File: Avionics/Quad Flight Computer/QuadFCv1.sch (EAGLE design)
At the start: 94 parts, among them J1 10104111_MICROUSBAB, J2 1050270001, SW1 2-1437565-9, U1 TM4C123GH6PZ, U2 74LVC4245APW, U3 ATMEGA32U2-MU, U4 SPI_PPM, U5 MPU-6000, U6 HMC5883LSMD, U7 MS5611-01BA, U8 74AUP1G19GW, U9 S25FL127S, X1 HWB, Y1 32.768KHZ, Y2 AWSCR-20.00CW-T, Y3 PRQC16.00SR5010X000

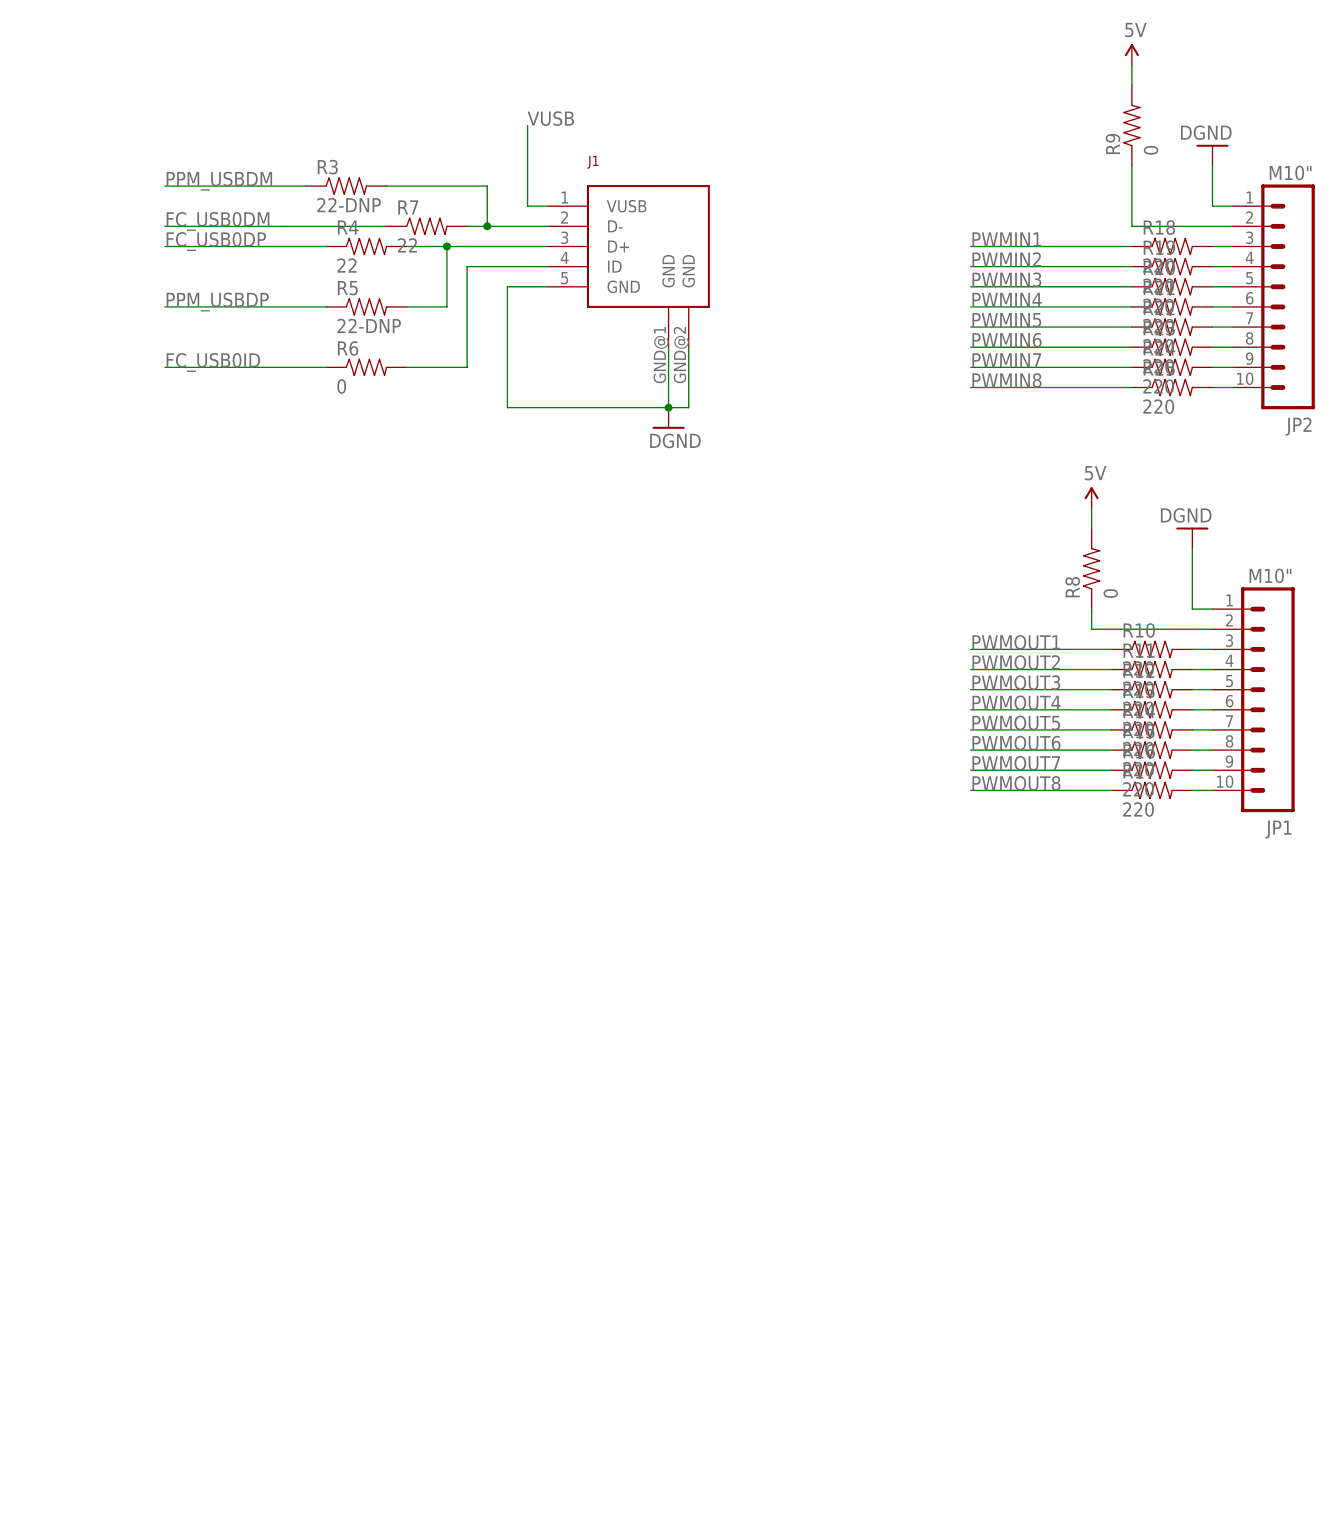
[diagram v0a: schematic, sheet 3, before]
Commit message: Added several connectors and modified power inputs to not immediately go to 5V plane.
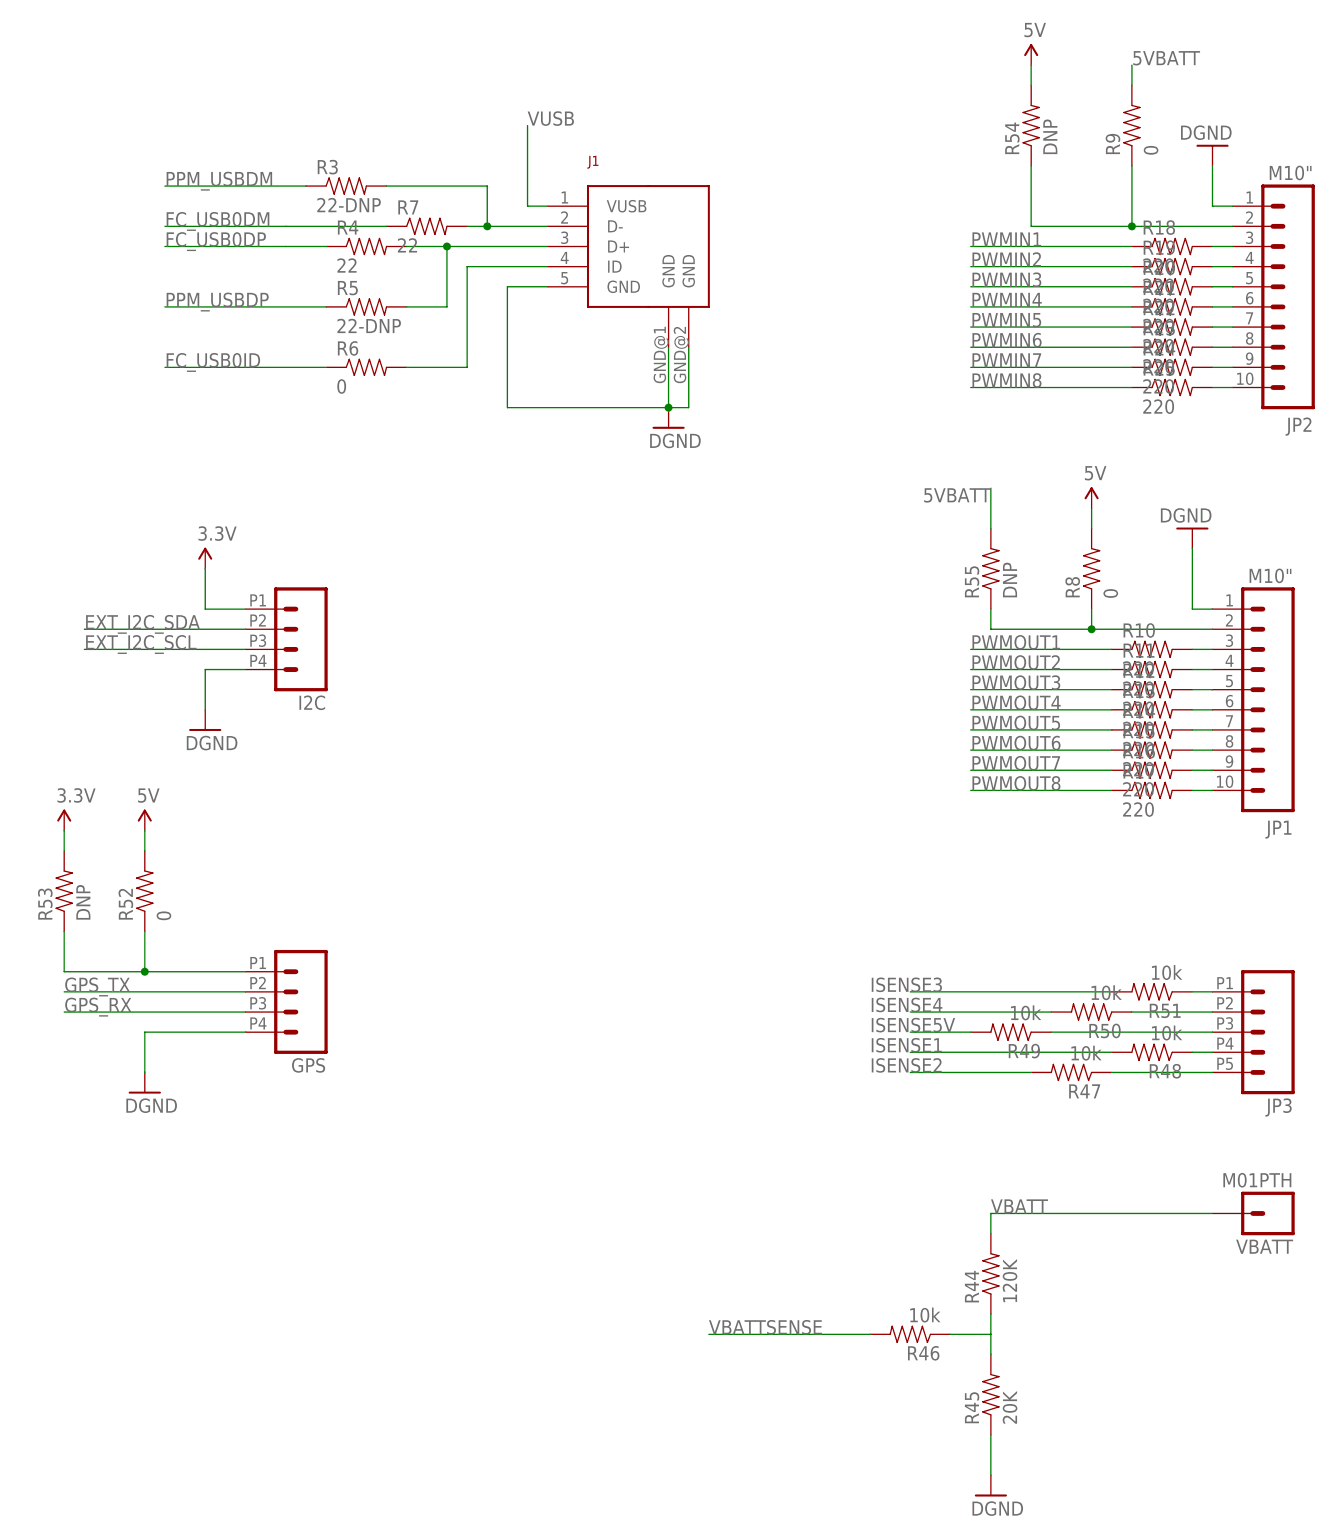
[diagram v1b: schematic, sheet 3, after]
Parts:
- added FC_JTAG: M04X2, SparkFun-Connectors:M04X2
- added GPS, I2C: (no value), Shared Libraries:M04DF13
- added JP3: (no value), Shared Libraries:M05DF13
- added R44: 120K, Shared Libraries:RESISTOR0603-RES
- added R45: 20K, Shared Libraries:RESISTOR0603-RES
- added R46, R47, R48, R49, R50, R51: 10k, Shared Libraries:RESISTOR0603-RES
- added R52: 0, Shared Libraries:RESISTOR0603-RES
- added R53: DNP, Shared Libraries:RESISTOR0603-RES
- added R54, R55: DNP, SparkFun-Resistors:RESISTOR0805-RES
- added VBATT: M01PTH, SparkFun-Connectors:M01PTH
- C15, C16, C17, C18: device SparkFun:CAP0402-CAP -> SparkFun:CAP0402
- R28, R29, R30, R31, R32, R33, R34, R35, R36, R37: device SparkFun:RESISTOR0402-RES -> SparkFun:RESISTOR0402
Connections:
- new net 5VBATT: R55.2, R9.2
- new net EXT_I2C_SCL: I2C.3
- new net EXT_I2C_SDA: I2C.2
- new net GPS_RX: GPS.3
- new net GPS_TX: GPS.2
- new net ISENSE1: R48.2
- new net ISENSE2: R47.2
- new net ISENSE3: R51.2
- new net ISENSE4: R50.2
- new net ISENSE5V: R49.2
- new net N$38: R44.1, R45.2, R46.1
- new net N$39: GPS.1, R52.1, R53.1
- new net N$44: JP3.1, R51.1
- new net N$45: JP3.2, R50.1
- new net N$46: JP3.3, R49.1
- new net N$47: JP3.4, R48.1
- new net N$48: JP3.5, R47.1
- new net VBATT: R44.2, VBATT.1
- new net VBATTSENSE: R46.2
- net 3.3V: now also FC_JTAG.4, I2C.1, R53.2
- net 5V: now also R52.2, R54.2; no longer R9.2
- net FC_JTAG_TCK: now also FC_JTAG.1
- net FC_JTAG_TDI: now also FC_JTAG.5
- net FC_JTAG_TDO: now also FC_JTAG.7
- net FC_JTAG_TMS: now also FC_JTAG.3
- net FC_RESET_L: now also FC_JTAG.2
- net GND: now also FC_JTAG.6, FC_JTAG.8, GPS.4, I2C.4, R45.1
- net N$23: now also R54.1
- net N$26: now also R55.1

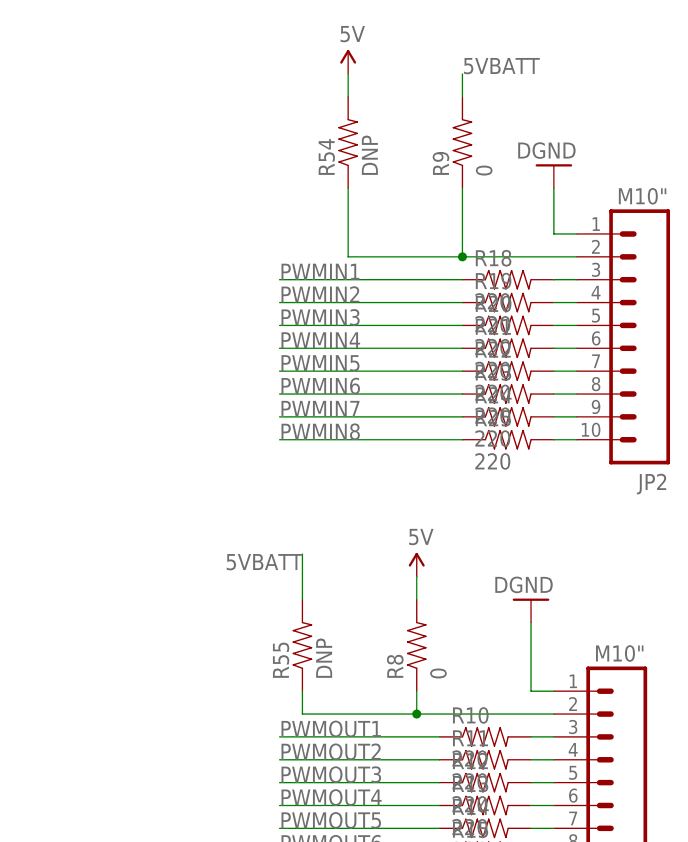
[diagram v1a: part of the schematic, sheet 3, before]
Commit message: Replaced all parts with 0402 packages to save board space.
I'm gonna need a smaller tweezers...
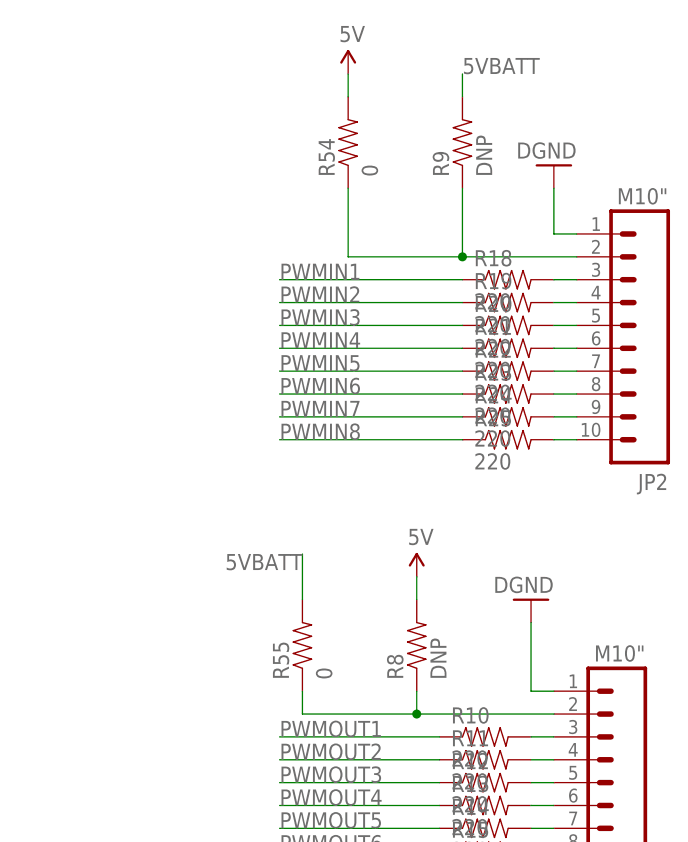
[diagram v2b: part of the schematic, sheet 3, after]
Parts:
- C1, C10, C11, C12, C13, C19, C2, C20, C21, C22, C23, C3, C4, C5, C6, C7, C8, C9: device SparkFun-Capacitors:CAP0603-CAP -> SparkFun-Capacitors:CAP0402-CAP
- C14: device SparkFun-Passives:CAP0603-CAP -> SparkFun-Capacitors:CAP0402-CAP
- C15, C16, C17, C18: device SparkFun:CAP0402 -> SparkFun-Capacitors:CAP0402-CAP
- R1, R10, R11, R12, R13, R14, R15, R16, R17, R18, R19, R2, R20, R21, R22, R23, R24, R25, R26, R27, R38, R39, R40, R41: device SparkFun-Resistors:RESISTOR0603-RES -> SparkFun-Resistors:RESISTOR0402-RES
- R28, R29, R30, R31, R32, R33, R34, R35, R36, R37: device SparkFun:RESISTOR0402 -> SparkFun-Resistors:RESISTOR0402-RES
- R3, R4, R42, R43, R44, R45, R46, R47, R48, R49, R5, R50, R51, R52, R53, R6, R7: device Shared Libraries:RESISTOR0603-RES -> SparkFun-Resistors:RESISTOR0402-RES
- R54, R55: value DNP -> 0; device SparkFun-Resistors:RESISTOR0805-RES -> SparkFun-Resistors:RESISTOR0402-RES
- R8, R9: value 0 -> DNP
